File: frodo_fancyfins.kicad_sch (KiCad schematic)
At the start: 58 parts, among them J1 Molex MicroFit 2x3, J2 Molex MicroFit 2x3, J3 U.FL, J4 SWD Header, Q1 NMOS, U1 STM32F072RBTx, U14 AS321KTR-G1, U15 AZ1117-5.0, U16 AZ1117-5.0, U2 MCP2562-E-SN, U3 AZ1117-3.3, Y1 8MHz 12pF

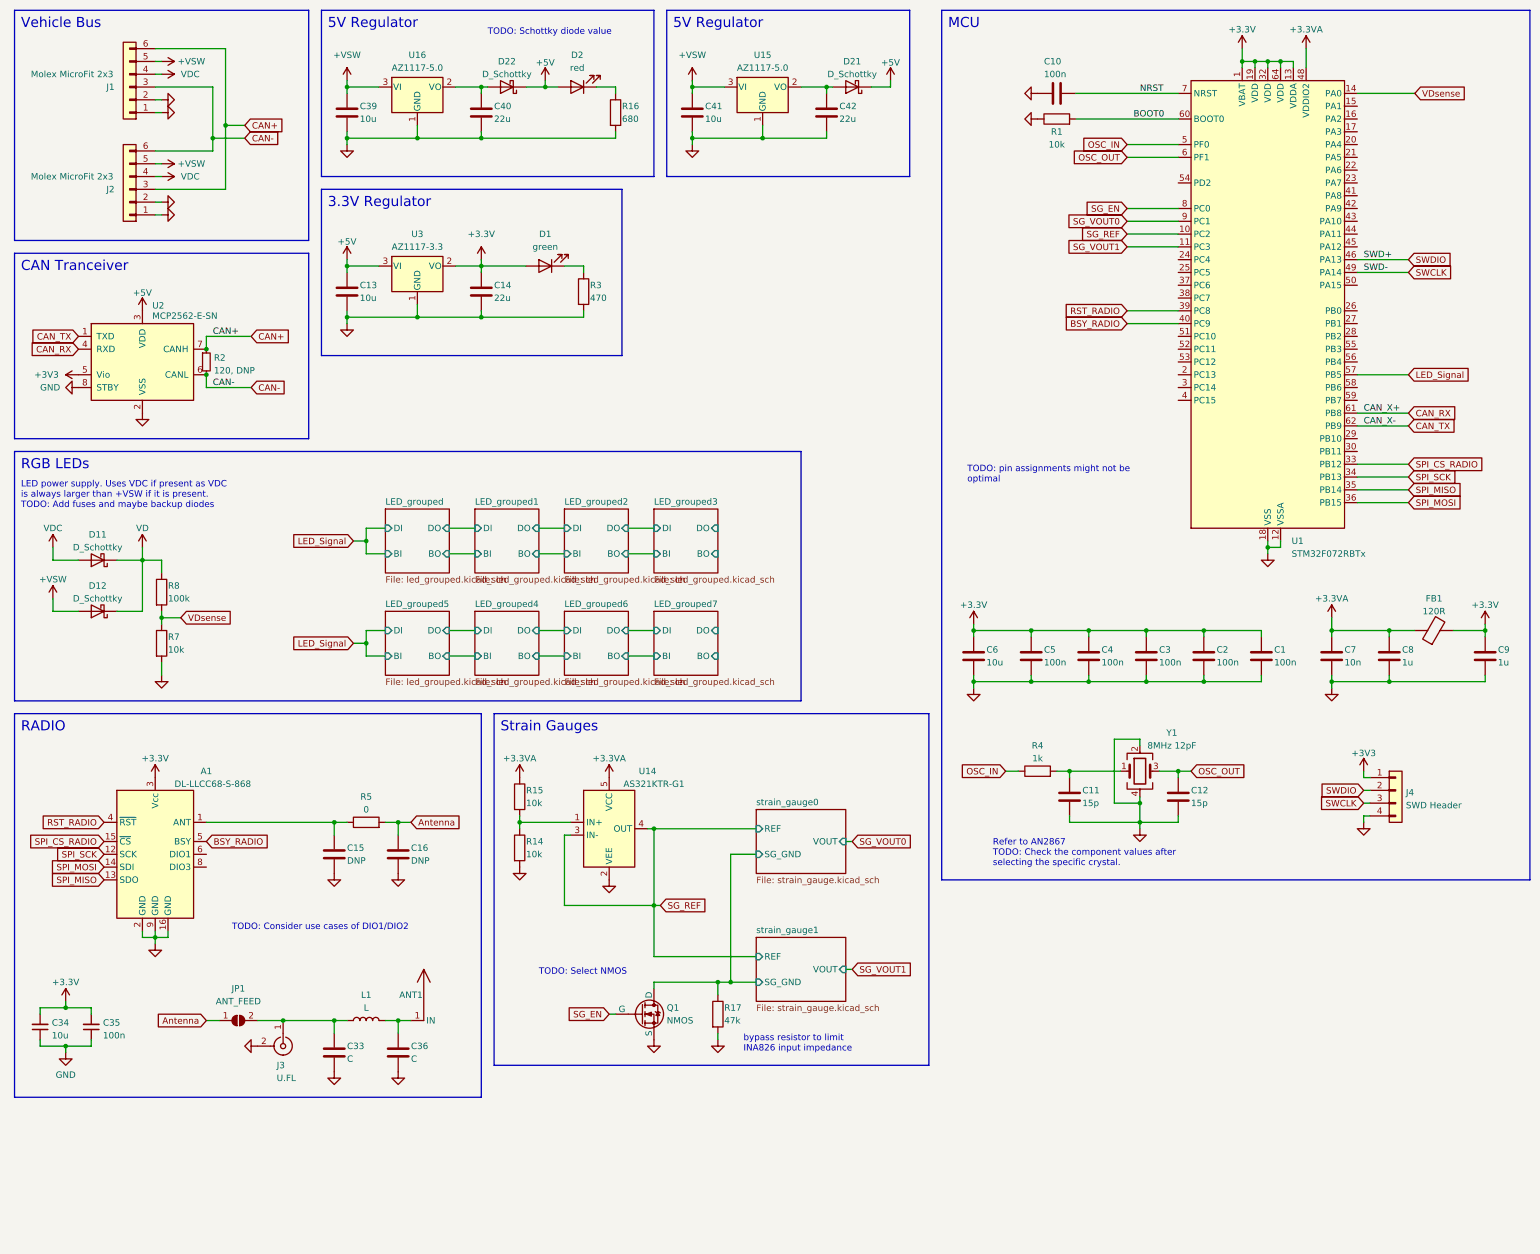
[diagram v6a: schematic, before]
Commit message: Add commentary concerning power supply
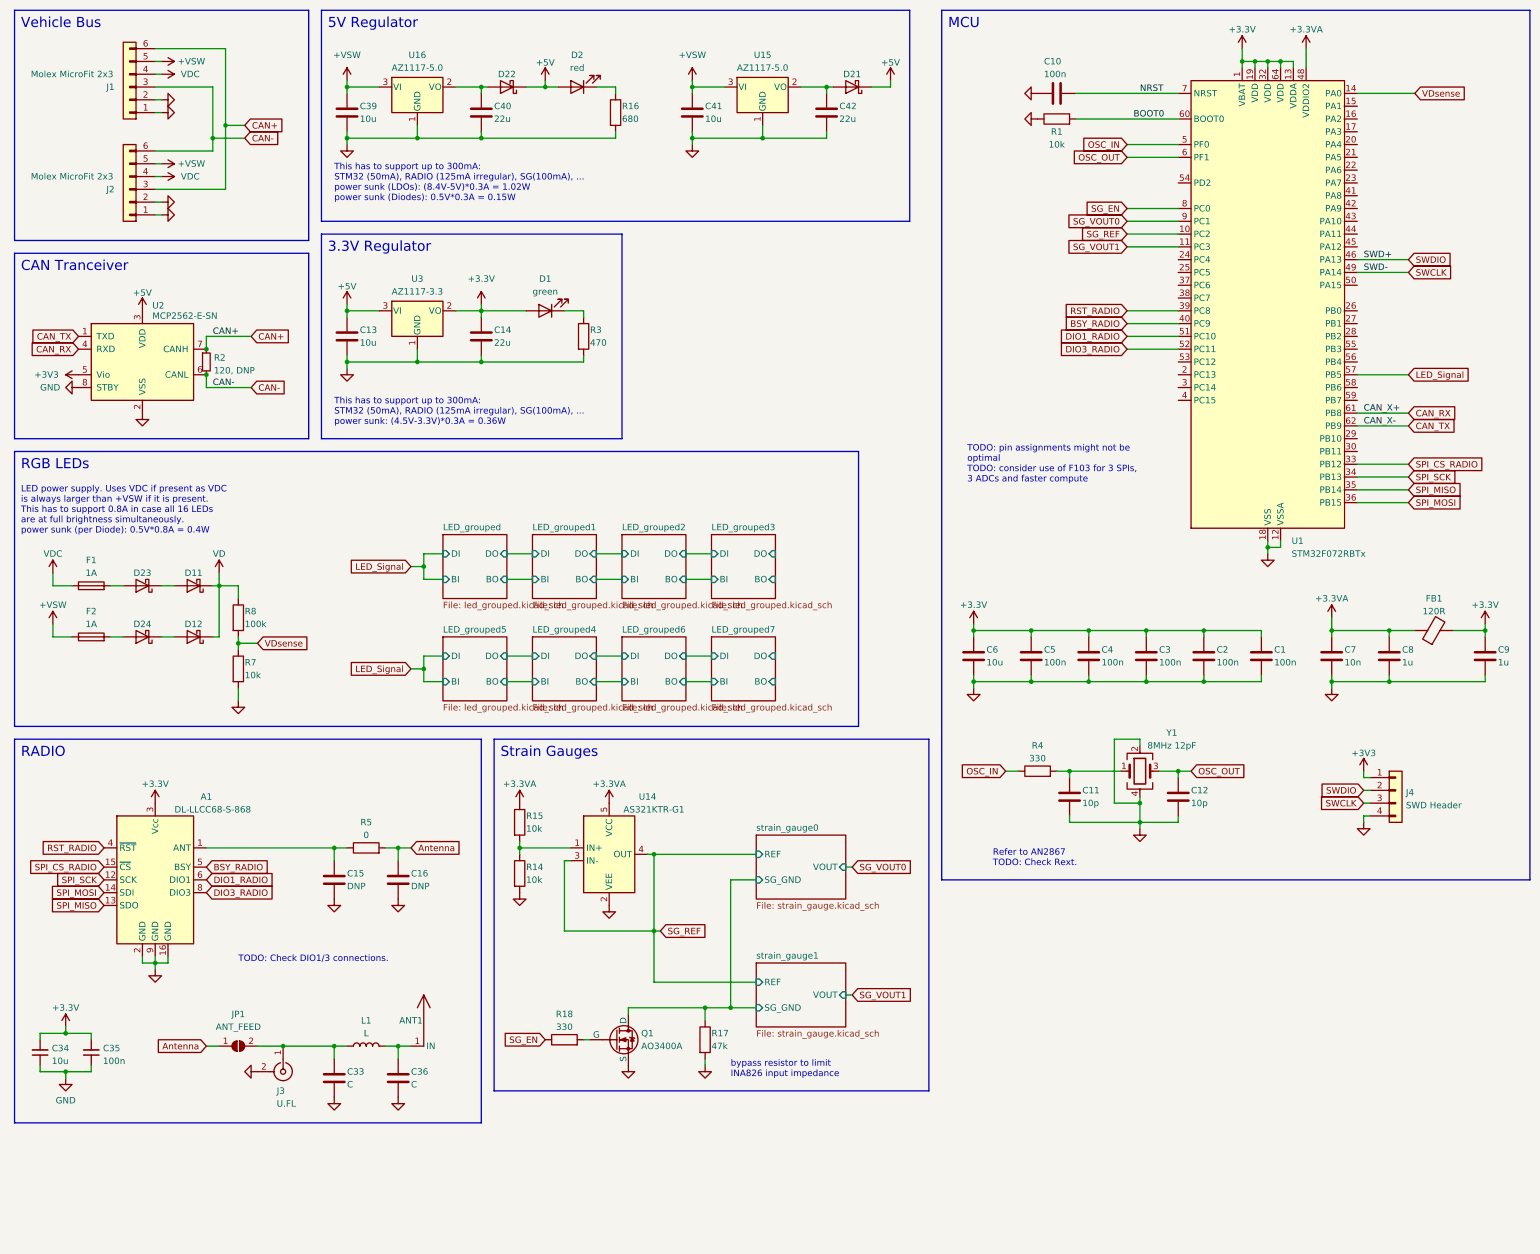
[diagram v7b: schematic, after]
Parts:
- added D23, D24: D_Schottky, symbol Device:D_Schottky
- added F1, F2: 1A, symbol Device:Fuse
- added R18: 330, symbol Device:R
- C11, C12: value 15p -> 10p
- Q1: value NMOS -> AO3400A
- R4: value 1k -> 330
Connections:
- net +VSW: now also F2.1; no longer D12.2 (A)
- net SG_EN: now also R18.1; no longer Q1.2 (G)
- net VDC: now also F1.1; no longer D11.2 (A)
- net DIO1_RADIO: now reaches U1.51 (PC10)
- net DIO1_RADIO: now also A1.6 (DIO1)
- net DIO3_RADIO: now reaches U1.52 (PC11)
- net DIO3_RADIO: now also A1.8 (DIO3)
- new net: D11.2 (A), D23.1 (K)
- new net: D23.2 (A), F1.2
- new net: D12.2 (A), D24.1 (K)
- new net: D24.2 (A), F2.2
- new net: Q1.2 (G), R18.2
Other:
- note added: "LED power supply. Uses VDC if present as VDC is always larger than +VSW if it is present. This has to support 0.8A in case all 16 LEDs are at full brightness simultaneously. power sunk (per Diode): 0.5V*0.8A = 0.4W"
- note added: "Refer to AN2867 TODO: Check Rext."
- note added: "TODO: Check DIO1/3 connections."
- note added: "TODO: pin assignments might not be optimal TODO: consider use of F103 for 3 SPIs, 3 ADCs and faster compute"
- note added: "This has to support up to 300mA: STM32 (50mA), RADIO (125mA irregular), SG(100mA), ... power sunk (LDOs): (8.4V-5V)*0.3A = 1.02W power sunk (Diodes): 0.5V*0.3A = 0.15W"
- note added: "This has to support up to 300mA: STM32 (50mA), RADIO (125mA irregular), SG(100mA), ... power sunk: (4.5V-3.3V)*0.3A = 0.36W"
- note removed: "LED power supply. Uses VDC if present as VDC is always larger than +VSW if it is present. TODO: Add fuses and maybe backup diodes"
- note removed: "Refer to AN2867 TODO: Check the component values after selecting the specific crystal."
- note removed: "TODO: Consider use cases of DIO1/DIO2"
- note removed: "TODO: Schottky diode value"
- note removed: "TODO: Select NMOS"
- note removed: "TODO: pin assignments might not be optimal"
- moved on the sheet: A1, ANT1, C13, C14, C15, C16, C33, C34, C35, C36, D1, D11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
